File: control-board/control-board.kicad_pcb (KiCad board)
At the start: 2 copper layers, 94.9 x 73 mm, 120 parts, among them J1 Conn_01x03, J10 DIN-4, J11 DIN-4, J12 Conn_01x03, J13 Conn_01x03, J14 Conn_01x02, J15 Conn_01x03, J16 Conn_01x02, J17 Conn_01x02, J18 Conn_01x02, J2 GPS_ANT, J3 LORA_ANT, J4 DIN-4, J5 DIN-4, J6 USB_C_Receptacle_USB2.0_16P, J7 Conn_01x03, J8 DIN-4, J9 DIN-4, Q1 2N7002, Q2 NXV90EPR, SW1 SW_SPST, U1 STM32H743VITx, U2 NEO-XM, U3 TCAN1462VDRQ1, U4 AMS1117-3.3, U6 AMS1117-3.3, U7 TCAN1462VDRQ1, Y1 8M, Y2 32.768k

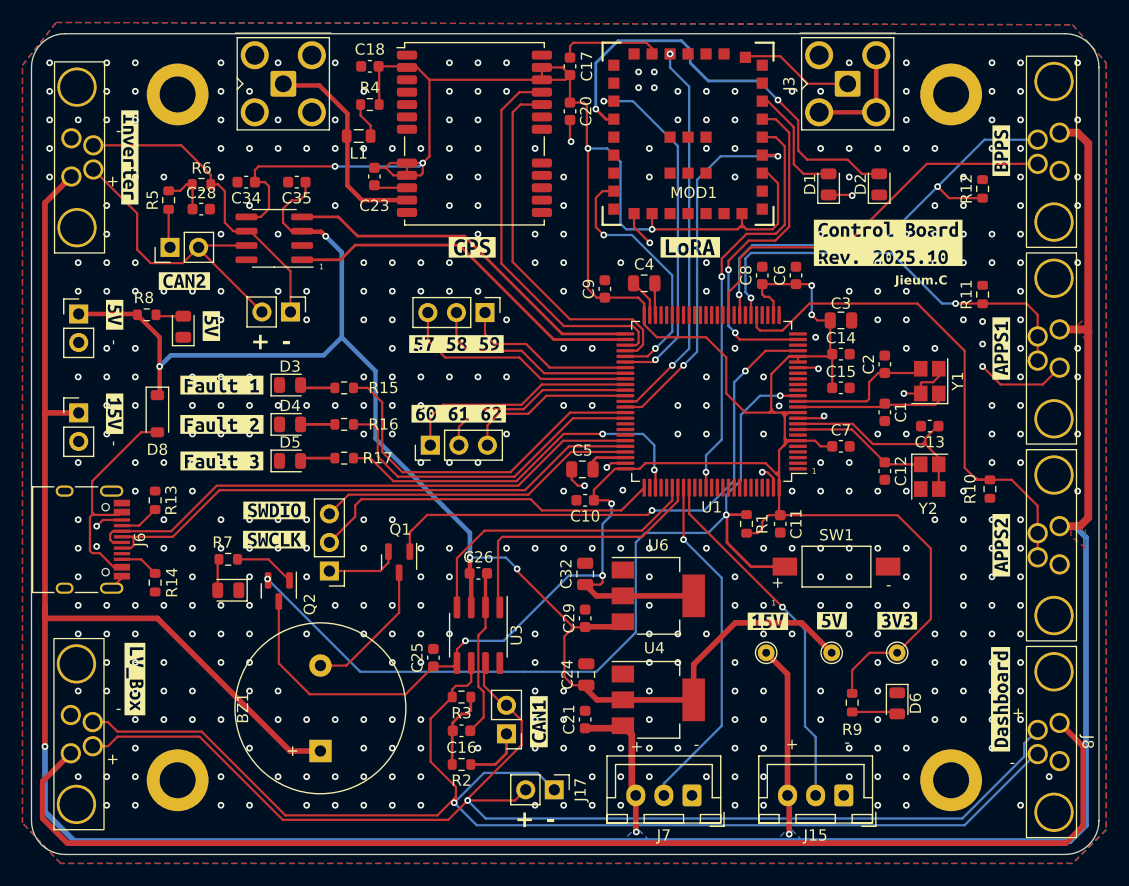
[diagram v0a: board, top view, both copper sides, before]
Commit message: fix: SWDIO LED
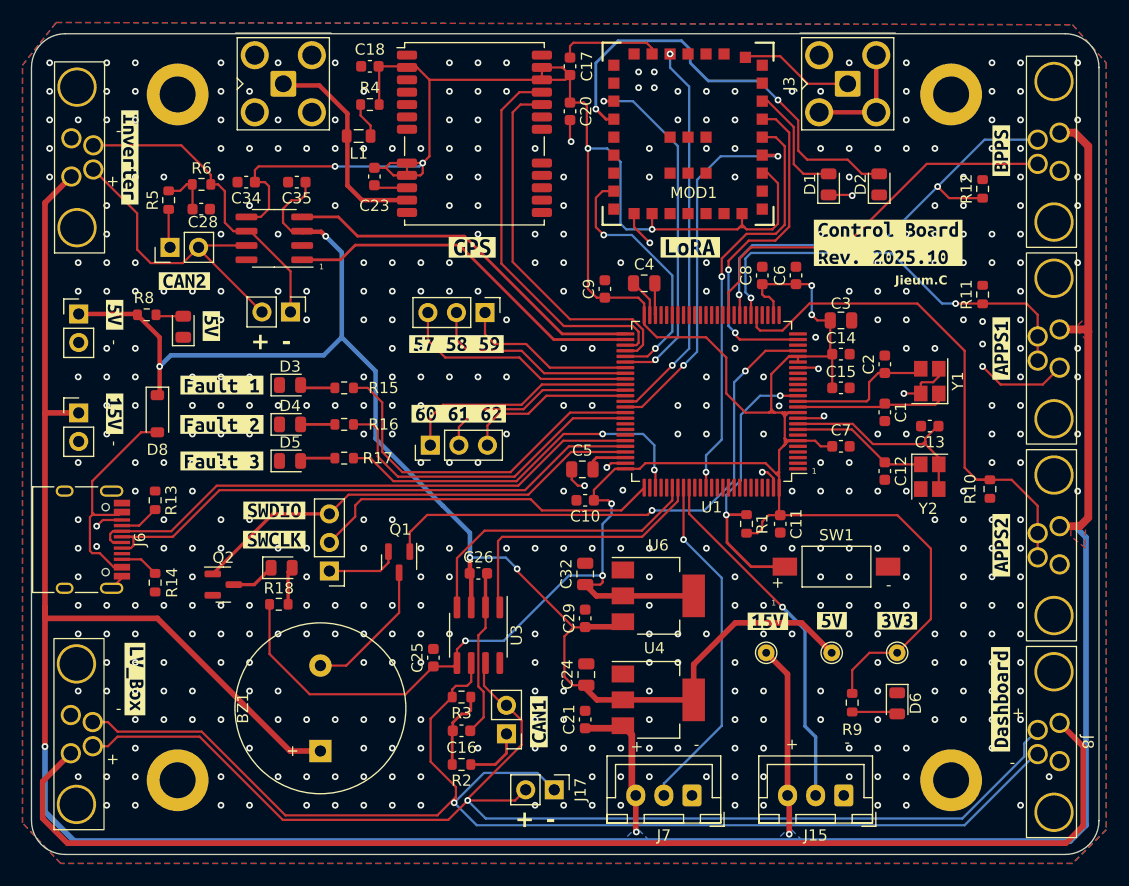
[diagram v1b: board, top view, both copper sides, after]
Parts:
- removed R7: 10k, Resistor_SMD:R_0603_1608Metric
- added R18: 10k, Resistor_SMD:R_0603_1608Metric, F.Cu at (132.0, 124.8)
- Q2: value NXV90EPR -> 2N7002
- moved D7 5.15 mm to (132.2, 121.5), turned to 0 degrees
- moved Q2 4.97 mm to (127.1, 123.0), turned to 0 degrees
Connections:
- D7 pad 1: GND -> Net-(D7-K)
- Q2 pad 1: Net-(Q2-D) -> SWDIO
- Q2 pad 2: NRST -> GND
- Q2 pad 3: +3V3 -> Net-(D7-K)
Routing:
- net NRST: track 80.2 -> 25.5 mm, vias 3 -> 2
- net SWDIO: track 28.6 -> 41.2 mm
- net Net-(Q2-D): track 5.40 -> 0.00 mm
- net Net-(D7-K): track 0.00 -> 3.93 mm
- net Net-(D7-A): track 2.80 -> 3.40 mm

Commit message: feat: add ESD in CAN
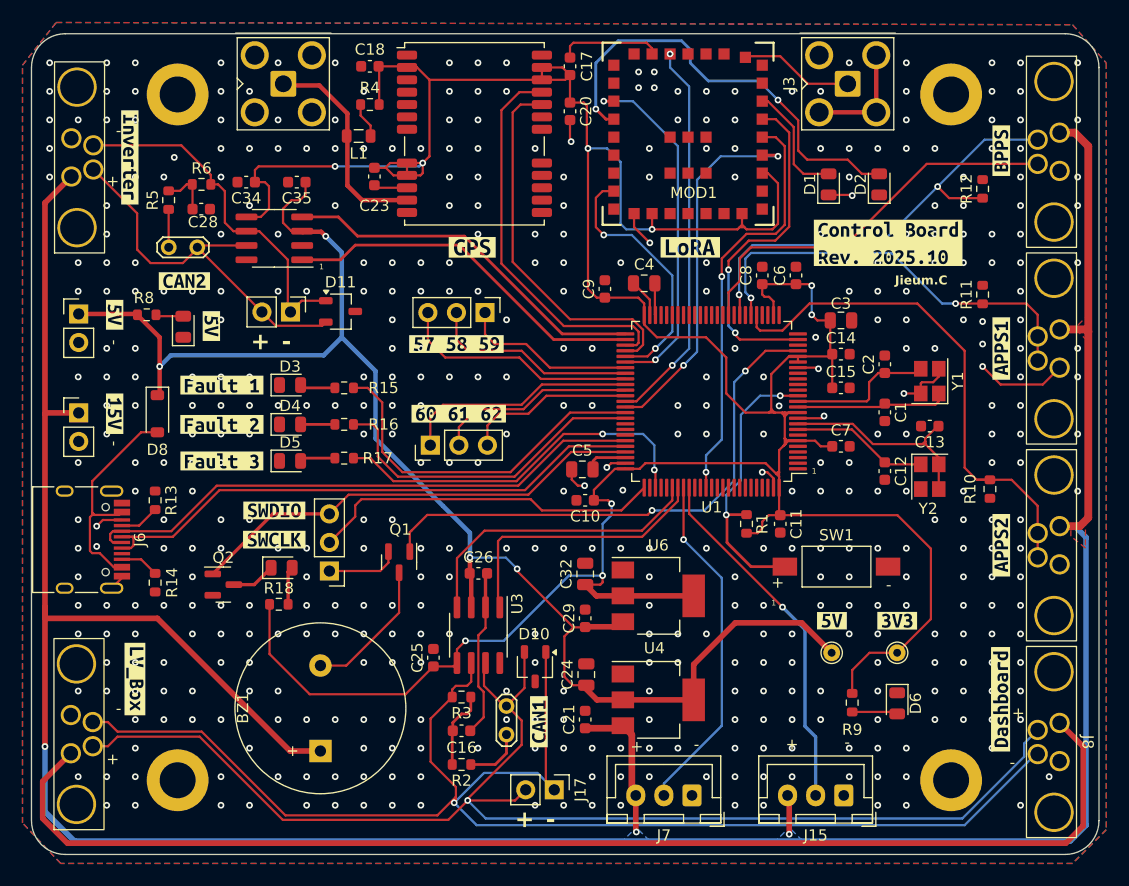
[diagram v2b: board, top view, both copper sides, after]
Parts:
- removed TP3: TP_15V, TestPoint:TestPoint_THTPad_D1.5mm_Drill0.7mm
- removed kibuzzard-68C831A8: G***, kibuzzard-68C831A8
- added D10: DESD2CAN2SOQ, Package_TO_SOT_SMD:TSOT-23, F.Cu at (154.8, 130.3)
- added D11: DESD2CAN2SOQ, Package_TO_SOT_SMD:TSOT-23, F.Cu at (137.5, 98.7)
- JP1, JP2: footprint Connector_PinHeader_2.54mm:PinHeader_1x02_P2.54mm_Vertical -> TestPoint:TestPoint_2Pads_Pitch2.54mm_Drill0.8mm
- moved JP1 2.47 mm to (152.2, 133.8), turned to -90 degrees
- moved JP2 2.42 mm to (124.8, 93.0), turned to 180 degrees
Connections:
- JP1 pad 1: Net-(JP1-A) -> CAN1_P
- JP1 pad 2: CAN1_P -> Net-(JP1-B)
- JP2 pad 1: Net-(JP2-A) -> CAN2_P
- JP2 pad 2: CAN2_P -> Net-(JP2-B)
- R2 pad 1: Net-(JP1-A) -> Net-(JP1-B)
- R5 pad 1: Net-(JP2-A) -> Net-(JP2-B)
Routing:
- net +15V: track 285.3 -> 271.8 mm
- net CAN1_N: track 117.9 -> 130.5 mm
- net CAN2_P: track 27.7 -> 34.0 mm
- net Net-(JP1-B): track 0.00 -> 5.70 mm
- net Net-(JP1-A): track 5.70 -> 0.00 mm
- net CAN1_P: track 114.2 -> 119.6 mm
- net CAN2_N: track 27.9 -> 32.0 mm
- net Net-(JP2-B): track 0.00 -> 3.43 mm
- net Net-(JP2-A): track 3.43 -> 0.00 mm
- net GND: vias 461 -> 467

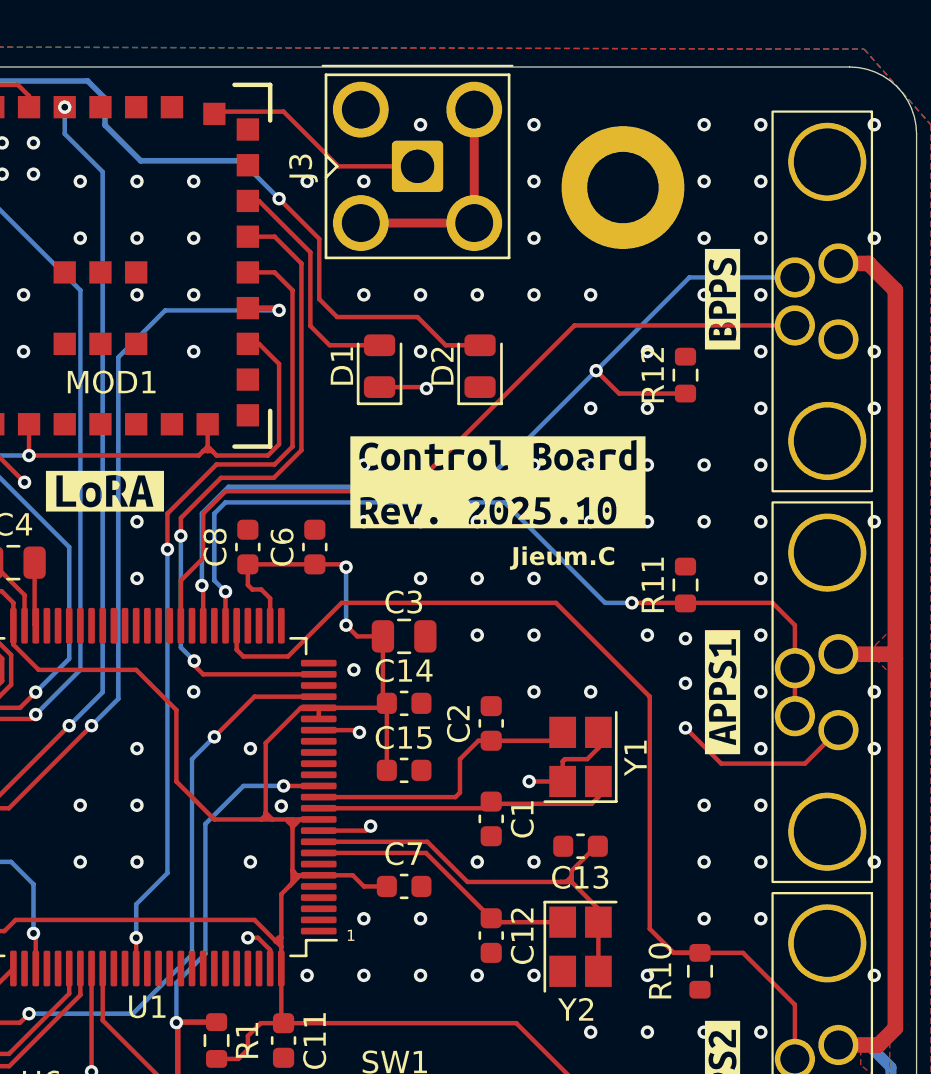
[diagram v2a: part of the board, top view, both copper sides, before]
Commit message: feat: update schematic & adc
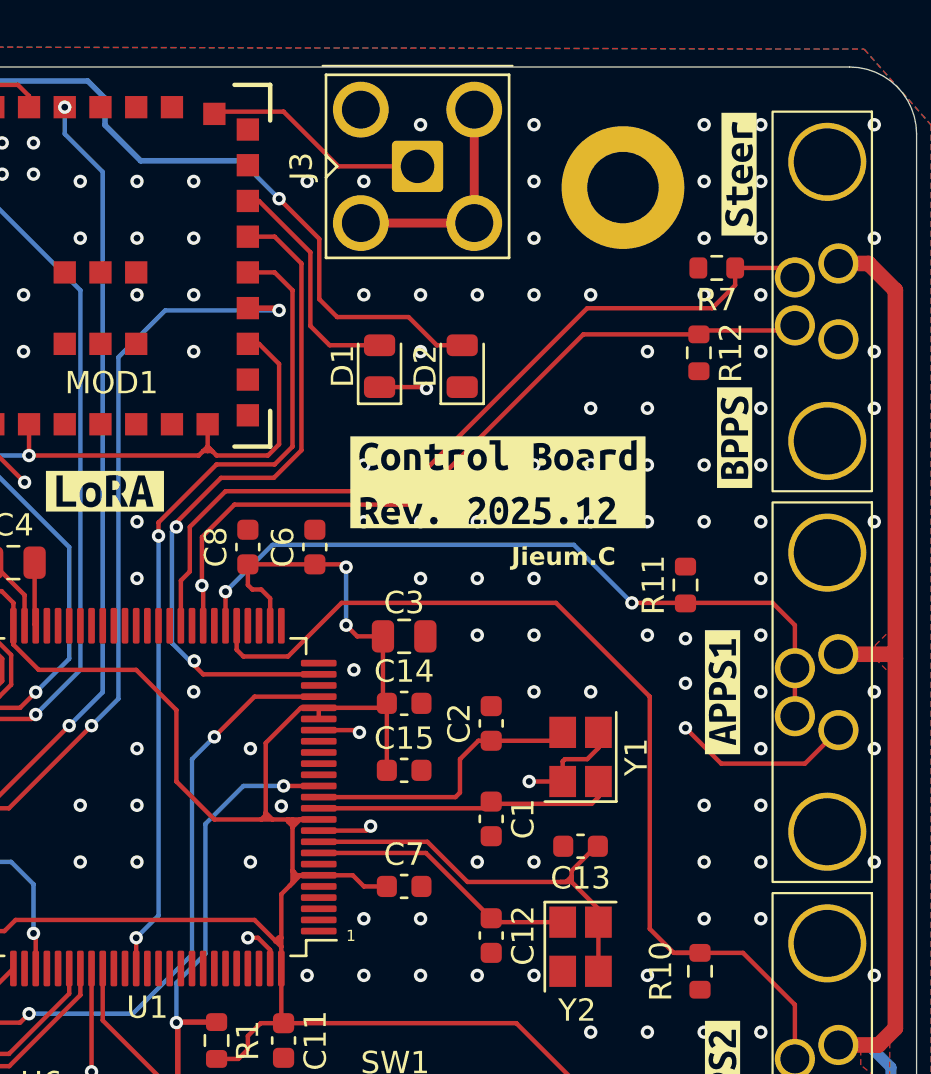
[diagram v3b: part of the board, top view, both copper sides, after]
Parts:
- removed kibuzzard-68E0D157: G***, kibuzzard-68E0D157
- added R7: 150R, Resistor_SMD:R_0603_1608Metric, F.Cu at (196.0, 83.0)
- added kibuzzard-6932874B: G***, kibuzzard-6932874B, F.Cu at (186.2, 92.6)
- added kibuzzard-6932882F: G***, kibuzzard-6932882F, F.Cu at (197.0, 78.8)
- moved kibuzzard-68C81C70 6.22 mm to (196.8, 90.6)
- moved R12 1.17 mm to (195.2, 86.8), turned to -90 degrees
- moved D2 0.80 mm to (184.6, 87.4)
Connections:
- net +15V renamed ctrl_pwr
- net VDC renamed dashboard_pwr
- J10 pad 2: ADC_BPPS -> ADC_STEER
- J10 pad 3: ADC_STEER -> ADC_BPPS
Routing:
- net ADC_BPPS: track 40.4 -> 34.5 mm, vias 2 -> 1
- net ADC_APPS2: track 37.8 -> 33.5 mm
- net ADC_STEER: track 35.4 -> 37.1 mm
- net Net-(D2-A): track 39.3 -> 38.5 mm
